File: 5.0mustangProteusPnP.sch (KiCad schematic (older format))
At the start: 6 parts, among them J2 5103308-3, J3 776228-1, J4 5103308-3, J5 776231-2, J6 776231-1, U1 FORD60PIN

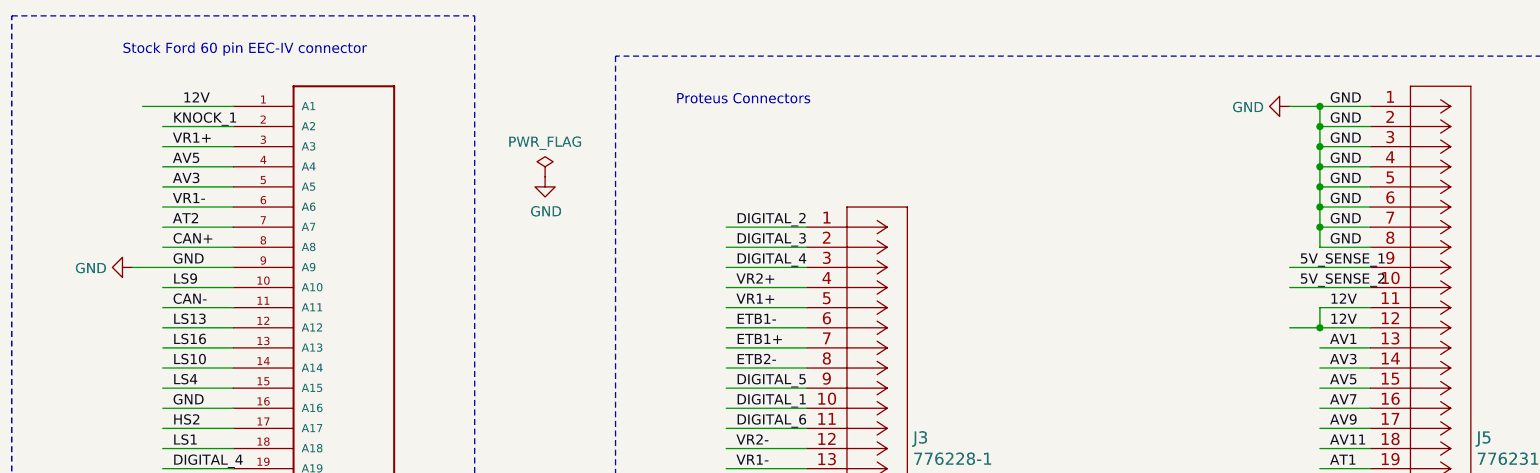
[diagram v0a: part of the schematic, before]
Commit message: changed 12V
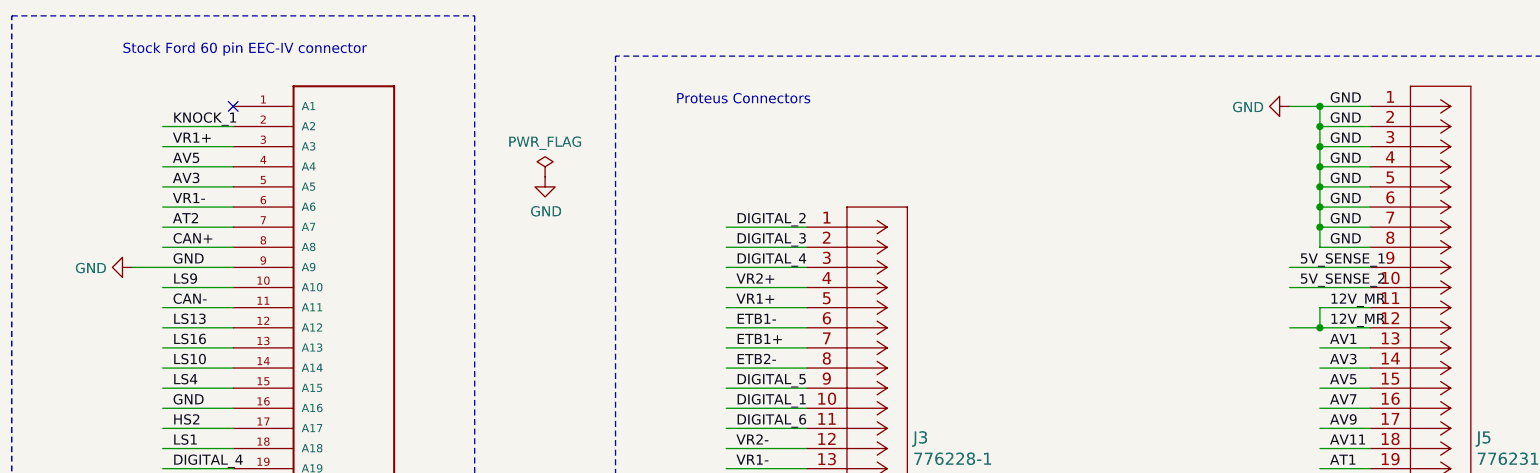
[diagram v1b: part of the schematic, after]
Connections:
- net labels removed: 12V
- wire segments 189 -> 188
- no-connect marks 10 -> 11
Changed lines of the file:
@@
 GND
 Text Label 7250 2000 0    50   ~ 0
-12V
+12V_MR
 Text Label 7250 2100 0    50   ~ 0
-12V
+12V_MR
 Text Label 7250 2200 0    50   ~ 0
 AV1
@@
 Text Label 6950 3000 0    50   ~ 0
 5V_SENSE_1
-Wire Wire Line
-	1800 1000 1350 1000
-Text Label 1550 1000 0    50   ~ 0
-12V
 $Comp
 L power:GND #PWR0102
@@
 Wire Notes Line
 	700  7250 700  550
+NoConn ~ 1800 1000
 $EndSCHEMATC

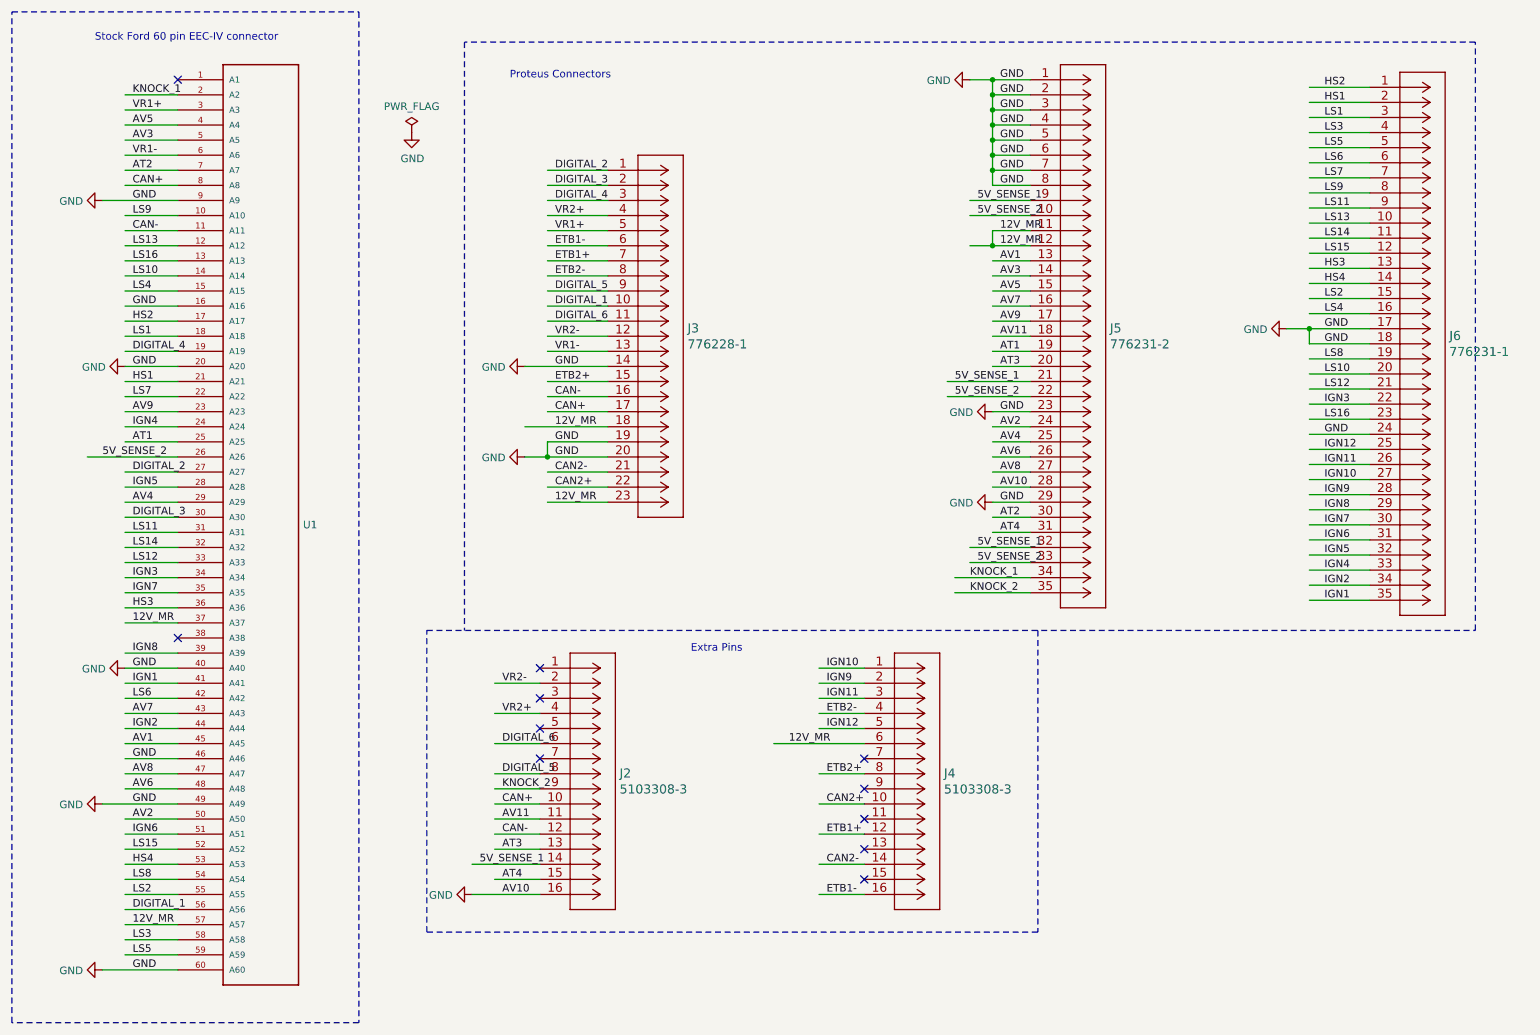
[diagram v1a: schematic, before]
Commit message: fixed 12V and IAC
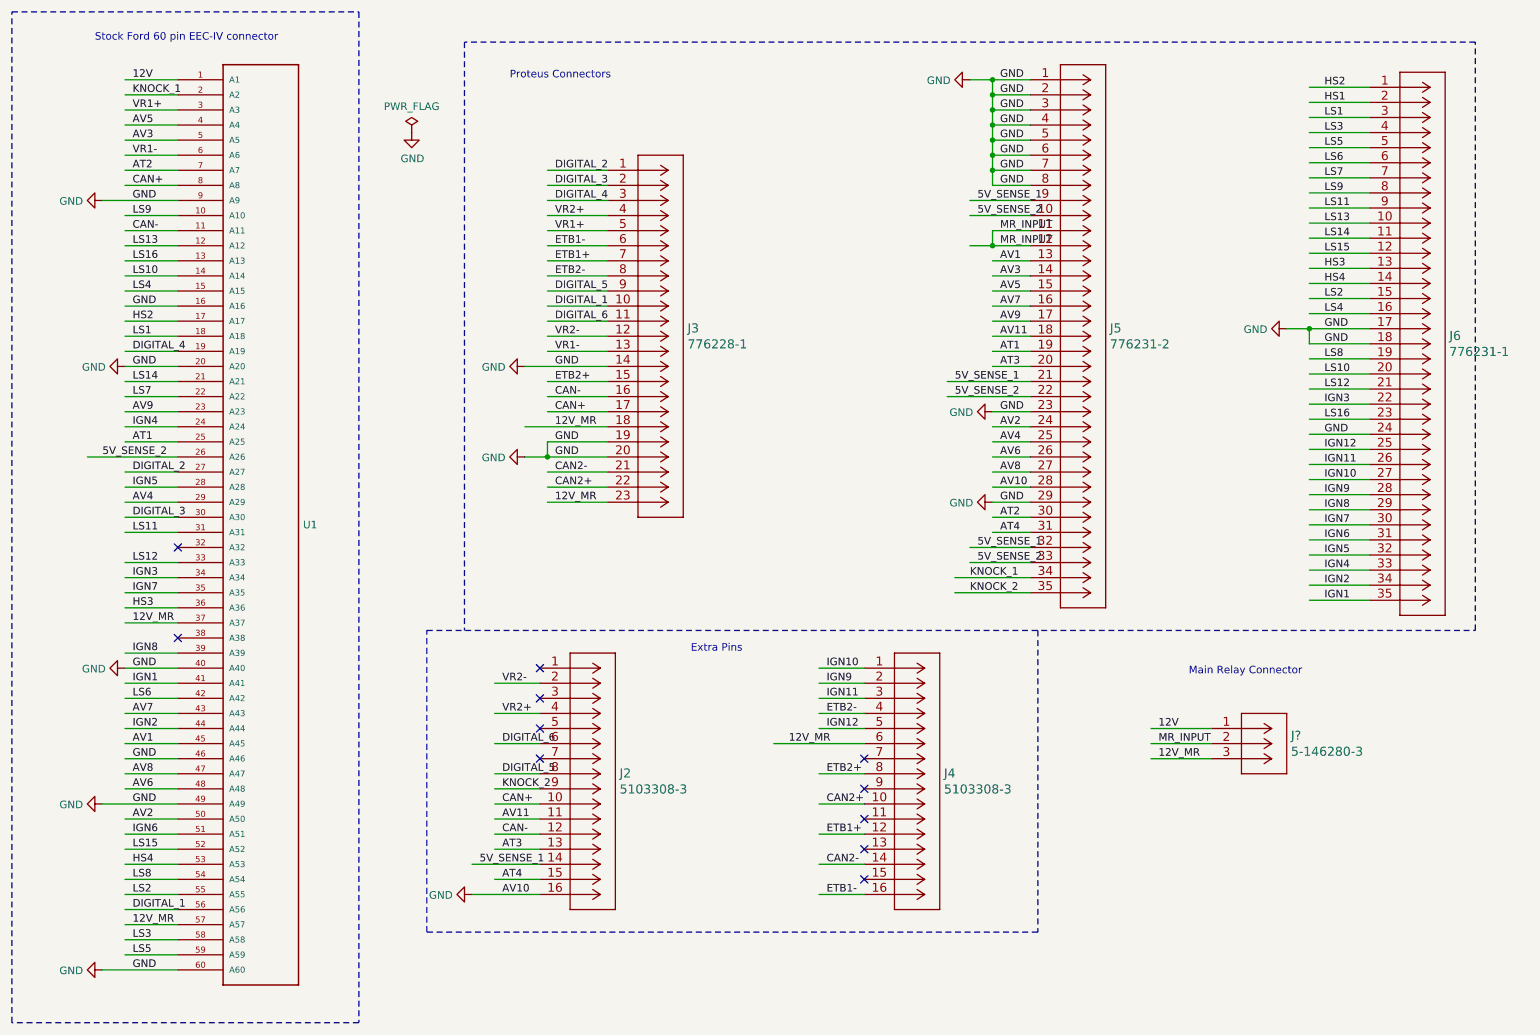
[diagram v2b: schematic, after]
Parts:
- added J?: 5-146280-3, CONN_5-146280-3_TYCO, symbol 5-146280-3:5-146280-3
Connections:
- net labels added: 12V, MR_INPUT
- wire segments 188 -> 191
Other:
- note added: "Main Relay Connector"
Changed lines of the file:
@@
 Comment4 ""
 $EndDescr
-$Comp
-L FORD60PIN:FORD60PIN U1
-U 1 1 5FF3D359
-P 1800 3500
-F 0 "U1" H 2630 3050 50  0000 L CNN
-F 1 "FORD60PIN" H 1800 3500 50  0001 L BNN
-F 2 "FORD60PIN:FORD60PIN" H 1800 3500 50  0001 L BNN
-F 3 "" H 1800 3500 50  0001 L BNN
-	1    1800 3500
-	1    0    0    -1
-$EndComp
 Wire Wire Line
 	1800 1100 1450 1100
@@
 Wire Wire Line
 	1800 4000 1450 4000
-Wire Wire Line
-	1800 4100 1450 4100
 Wire Wire Line
 	1800 4200 1450 4200
@@
 GND
 Text Label 7250 2000 0    50   ~ 0
-12V_MR
+MR_INPUT
 Text Label 7250 2100 0    50   ~ 0
-12V_MR
+MR_INPUT
 Text Label 7250 2200 0    50   ~ 0
 AV1
@@
 GND
 Text Label 1500 3000 0    50   ~ 0
-HS1
+LS14
 Text Label 1500 3100 0    50   ~ 0
 LS7
@@
 Text Label 1500 4000 0    50   ~ 0
 LS11
-Text Label 1500 4100 0    50   ~ 0
-LS14
 Text Label 1500 4200 0    50   ~ 0
 LS12
@@
 Wire Notes Line
 	700  7250 700  550
-NoConn ~ 1800 1000
+Wire Wire Line
+	8650 5300 8250 5300
+Wire Wire Line
+	8650 5400 8250 5400
+Wire Wire Line
+	8650 5500 8250 5500
+Text Label 8300 5400 0    50   ~ 0
+MR_INPUT
+Text Label 8300 5300 0    50   ~ 0
+12V
+Text Label 8300 5500 0    50   ~ 0
+12V_MR
+$Comp
+L FORD60PIN:FORD60PIN U1
+U 1 1 5FF3D359
+P 1800 3500
+F 0 "U1" H 2630 3050 50  0000 L CNN
+F 1 "FORD60PIN" H 1800 3500 50  0001 L BNN
+F 2 "FORD60PIN:FORD60PIN" H 1800 3500 50  0001 L BNN
+F 3 "" H 1800 3500 50  0001 L BNN
+	1    1800 3500
+	1    0    0    -1
+$EndComp
+Wire Wire Line
+	1800 1000 1450 1000
+Text Label 1500 1000 0    50   ~ 0
+12V
+Text Notes 8500 4950 0    50   ~ 0
+Main Relay Connector
+NoConn ~ 1800 4100
+$Comp
+L 5-146280-3:5-146280-3 J?
+U 1 1 5FFFBBB6
+P 8650 5300
+F 0 "J?" H 9178 5253 60  0000 L CNN
+F 1 "5-146280-3" H 9178 5147 60  0000 L CNN
+F 2 "CONN_5-146280-3_TYCO" H 9050 5140 60  0001 C CNN
+F 3 "" H 8650 5300 60  0000 C CNN
+	1    8650 5300
+	1    0    0    -1
+$EndComp
 $EndSCHEMATC

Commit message: fixed CEL assign
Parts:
- J1: renamed from J?; footprint CONN_5-146280-3_TYCO -> 5-146280-3:5-146280-3
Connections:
- wire segments 191 -> 192
- no-connect marks 11 -> 10
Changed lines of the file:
@@
 	1800 4000 1450 4000
-Wire Wire Line
-	1800 4200 1450 4200
 Wire Wire Line
 	1800 4300 1450 4300
@@
 GND
 Text Label 1500 2600 0    50   ~ 0
-HS2
+LS12
 Text Label 1500 2700 0    50   ~ 0
 LS1
@@
 Text Label 1500 4000 0    50   ~ 0
 LS11
-Text Label 1500 4200 0    50   ~ 0
-LS12
 Text Label 1500 4300 0    50   ~ 0
 IGN3
@@
 Text Label 6100 6400 0    50   ~ 0
 ETB1-
-NoConn ~ 4200 4900
 NoConn ~ 4200 5100
 NoConn ~ 4200 5300
-NoConn ~ 6350 5500
 NoConn ~ 6350 5700
 NoConn ~ 6350 5900
@@
 NoConn ~ 1800 4100
 $Comp
-L 5-146280-3:5-146280-3 J?
+L 5-146280-3:5-146280-3 J1
 U 1 1 5FFFBBB6
 P 8650 5300
-F 0 "J?" H 9178 5253 60  0000 L CNN
+F 0 "J1" H 9178 5253 60  0000 L CNN
 F 1 "5-146280-3" H 9178 5147 60  0000 L CNN
-F 2 "CONN_5-146280-3_TYCO" H 9050 5140 60  0001 C CNN
+F 2 "5-146280-3:5-146280-3" H 9050 5140 60  0001 C CNN
 F 3 "" H 8650 5300 60  0000 C CNN
 	1    8650 5300
 	1    0    0    -1
 $EndComp
+Wire Wire Line
+	4200 4900 3900 4900
+Text Label 3950 4900 0    50   ~ 0
+HS1
+NoConn ~ 1800 4200
+Wire Wire Line
+	6350 5500 6050 5500
+Text Label 6100 5500 0    50   ~ 0
+HS2
 $EndSCHEMATC
